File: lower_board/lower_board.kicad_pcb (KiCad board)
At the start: 2 copper layers, 71 parts, among them J1 Conn_01x04, J2 Conn_01x04, J3 Conn_01x03, SW1 SW_Push, SW10 SW_Push, SW11 SW_Push, SW12 SW_Push, SW13 SW_Push, SW14 SW_Push, SW15 SW_Push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

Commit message: lower board component placement
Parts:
- moved D23 262.1 mm to (73.2, 109.9)
- moved D24 261.5 mm to (73.2, 128.9)
- moved D22 260.1 mm to (73.2, 90.8)
- moved D21 259.0 mm to (73.2, 71.8)
- moved D25 242.3 mm to (92.3, 71.8)
- moved SW8 241.8 mm to (70.0, 120.5)
- moved D28 241.8 mm to (92.3, 128.9)
- moved D26 241.7 mm to (92.3, 90.8)
- moved D27 241.1 mm to (92.3, 109.9)
- moved SW6 240.8 mm to (70.0, 82.3)
- moved SW7 240.3 mm to (70.0, 101.4)
- moved SW5 239.4 mm to (70.0, 63.3)
- moved H1 236.8 mm to (41.5, 138.4)
- moved D29 233.1 mm to (111.3, 71.8)
- moved D31 231.9 mm to (111.3, 109.9)
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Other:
- board outline added: 96.5 x 96.5 mm
- board text added: "TODO: -ALIGN SWITCHES WITH HOLES -ROUTING -PLACE J3"

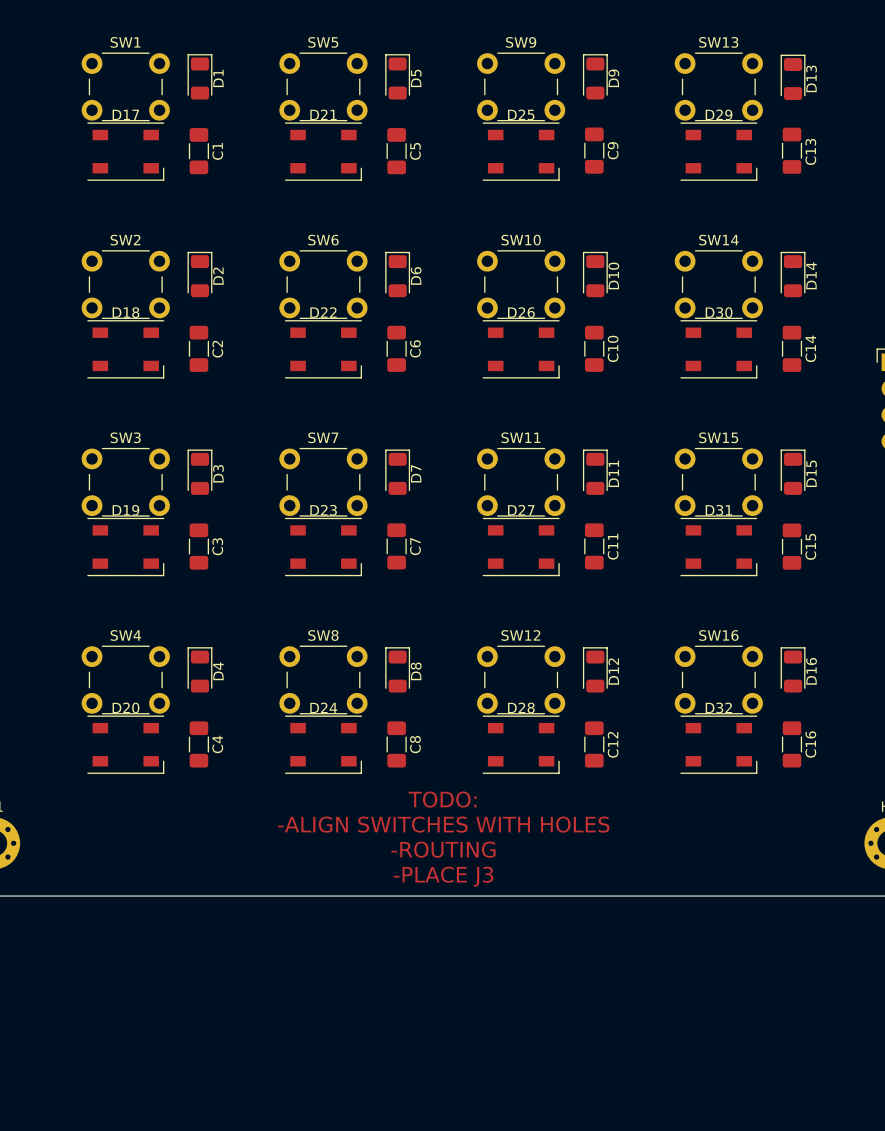
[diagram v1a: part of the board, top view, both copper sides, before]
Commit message: Lower board routing
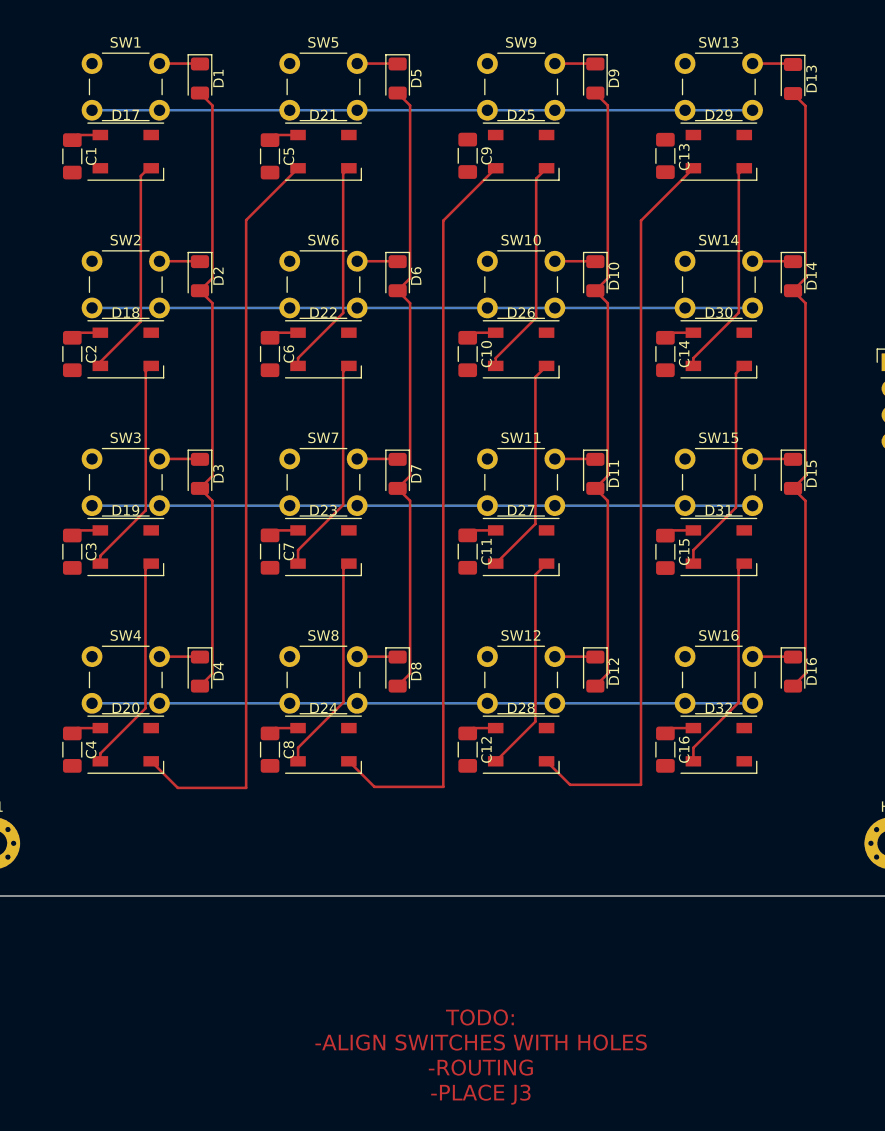
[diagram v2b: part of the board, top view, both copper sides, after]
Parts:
- moved C1 12.2 mm to (49.0, 72.2)
- moved C13 12.2 mm to (106.2, 72.2)
- moved C14 12.2 mm to (106.2, 91.3)
- moved C15 12.2 mm to (106.2, 110.4)
- moved C16 12.2 mm to (106.2, 129.4)
- moved C2 12.2 mm to (49.0, 91.3)
- moved C3 12.2 mm to (49.0, 110.3)
- moved C4 12.2 mm to (49.0, 129.4)
- moved C5 12.2 mm to (68.1, 72.2)
- moved C6 12.2 mm to (68.1, 91.3)
- moved C7 12.2 mm to (68.1, 110.3)
- moved C8 12.2 mm to (68.1, 129.4)
- moved C10 12.2 mm to (87.2, 91.3)
- moved C11 12.2 mm to (87.2, 110.3)
- moved C12 12.2 mm to (87.2, 129.4)
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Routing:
- net Net-(D20-Pad1): track 0.00 -> 72.0 mm
- net Net-(D24-Pad1): track 0.00 -> 71.8 mm
- net Net-(D28-Pad1): track 0.00 -> 71.5 mm
- net /ROW3: track 0.00 -> 63.6 mm
- net /ROW2: track 0.00 -> 63.6 mm
- net /ROW1: track 0.00 -> 63.6 mm
- net /ROW0: track 0.00 -> 63.6 mm
- net /COL2: track 0.00 -> 60.1 mm
- net /COL0: track 0.00 -> 60.1 mm
- net /COL1: track 0.44 -> 60.6 mm
- net /COL3: track 0.00 -> 60.1 mm
- net VSS: track 0.00 -> 40.7 mm
- net Net-(D17-Pad1): track 0.00 -> 21.2 mm
- net Net-(D30-Pad1): track 0.00 -> 21.1 mm
- net Net-(D21-Pad1): track 0.00 -> 21.1 mm
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
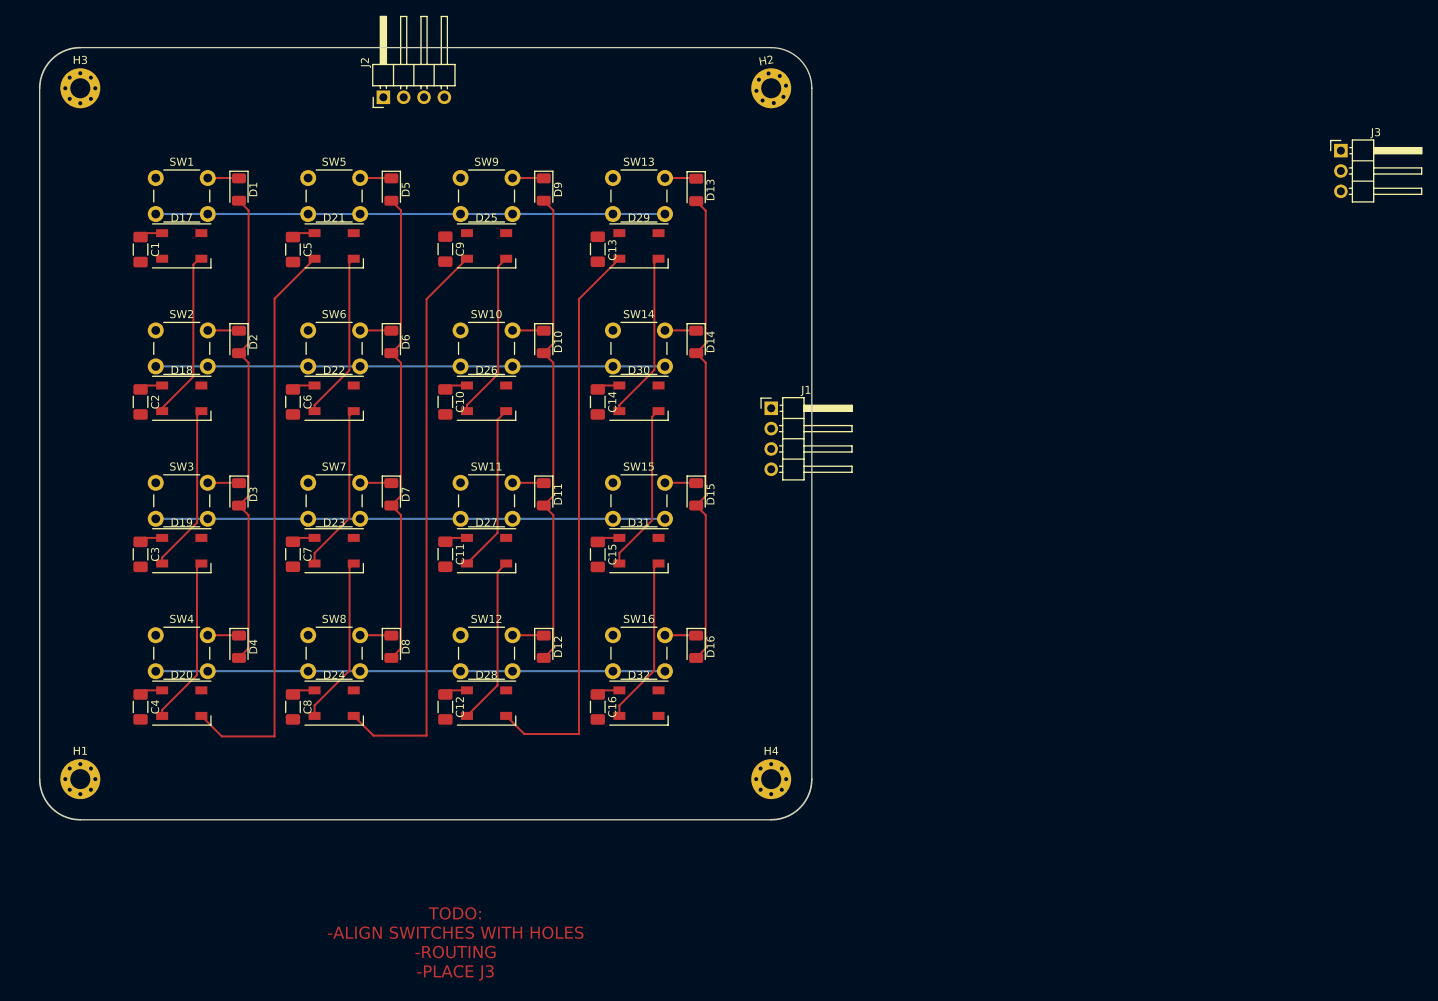
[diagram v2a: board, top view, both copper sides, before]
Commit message: Upgraded projects to KiCAD 7 Finished routing Added BOMs
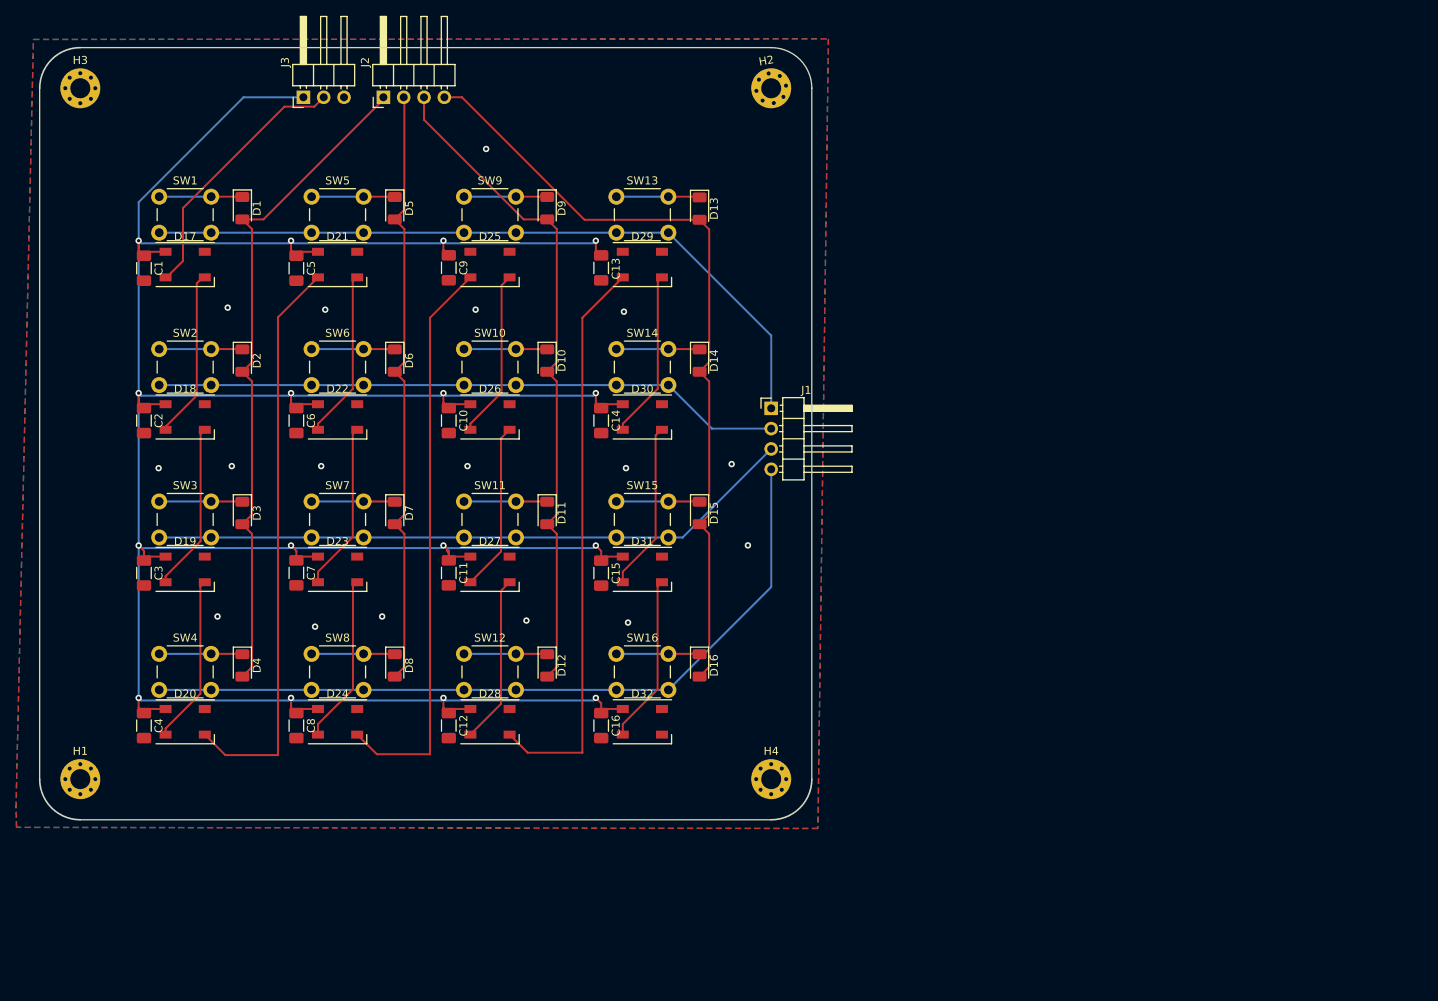
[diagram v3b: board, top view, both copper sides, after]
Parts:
- moved J3 129.9 mm to (69.4, 53.2), turned to 90 degrees
- moved SW10 2.37 mm to (89.5, 84.7)
- moved SW14 2.37 mm to (108.5, 84.7)
- moved SW6 2.37 mm to (70.4, 84.7)
- moved SW2 2.37 mm to (51.4, 84.7)
- moved C5 2.37 mm to (68.5, 74.6)
- moved C6 2.37 mm to (68.5, 93.6)
- moved C7 2.37 mm to (68.5, 112.7)
- moved C8 2.37 mm to (68.5, 131.7)
- moved D13 2.37 mm to (118.9, 67.1)
- moved D14 2.37 mm to (118.9, 86.1)
- moved D15 2.37 mm to (118.9, 105.2)
- moved D16 2.37 mm to (118.9, 124.2)
- moved D21 2.37 mm to (73.7, 74.1)
- moved D22 2.37 mm to (73.7, 93.2)
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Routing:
- net VSS: track 40.7 -> 396.1 mm, vias 0 -> 16
- net /COL3: track 60.1 -> 98.3 mm
- net /DIN: track 0.00 -> 33.0 mm
- net /ROW3: track 63.6 -> 96.6 mm
- net /ROW0: track 63.6 -> 90.9 mm
- net /COL0: track 60.1 -> 84.2 mm
- net /COL2: track 60.1 -> 83.5 mm
- net /ROW2: track 63.6 -> 81.1 mm
- net /COL1: track 60.6 -> 76.4 mm
- net /ROW1: track 63.6 -> 78.8 mm
- net Net-(D4-Pad1): track 3.92 -> 10.4 mm
- net Net-(D3-Pad1): track 3.92 -> 10.4 mm
- net Net-(D16-Pad1): track 3.92 -> 10.4 mm
- net Net-(D15-Pad1): track 3.92 -> 10.4 mm
- net Net-(D13-Pad1): track 3.94 -> 10.4 mm
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- added copper zone on B.Cu, net GND
- added copper zone on F.Cu, net GND
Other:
- board text added: "ARP"
- board text added: "Lower Deck"
- board text removed: "TODO: -ALIGN SWITCHES WITH HOLES -ROUTING -PLACE J3"
